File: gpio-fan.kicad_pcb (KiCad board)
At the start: 2 copper layers, 36 x 30.8 mm, 38 parts, among them J1 Conn_01x05, J10 Conn_01x04 DNS, J2 Conn_01x05 DNS, J3 Conn_01x02, J4 Conn_02x07_Odd_Even, J5 Conn_01x04 DNS, J6 Conn_01x02, J7 Conn_01x02 DNS, J8 Conn_01x02 DNS, J9 Conn_01x04 DNS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

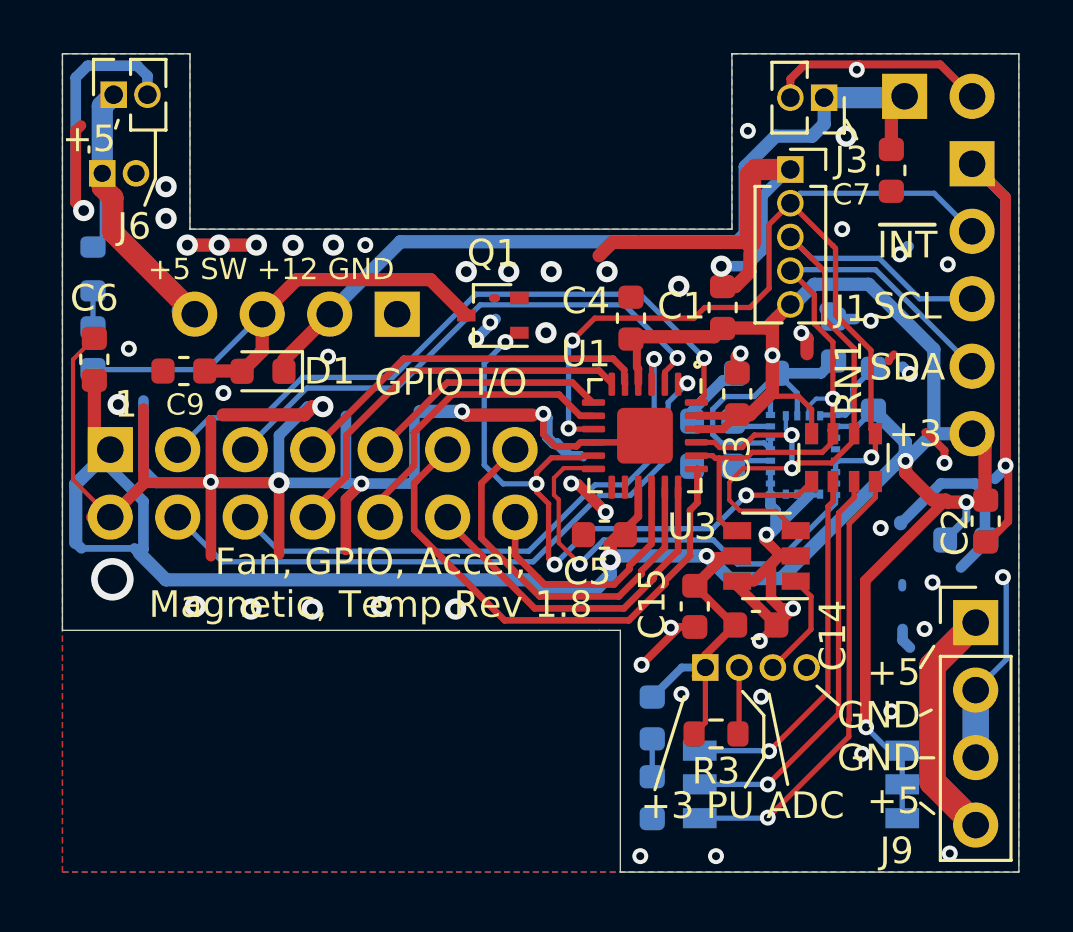
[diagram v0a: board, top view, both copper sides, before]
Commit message: V1.9, changed U2 to Bosch BMX180
Signed-off-by: Aaron Williams <aaron.w2@gmail.com>
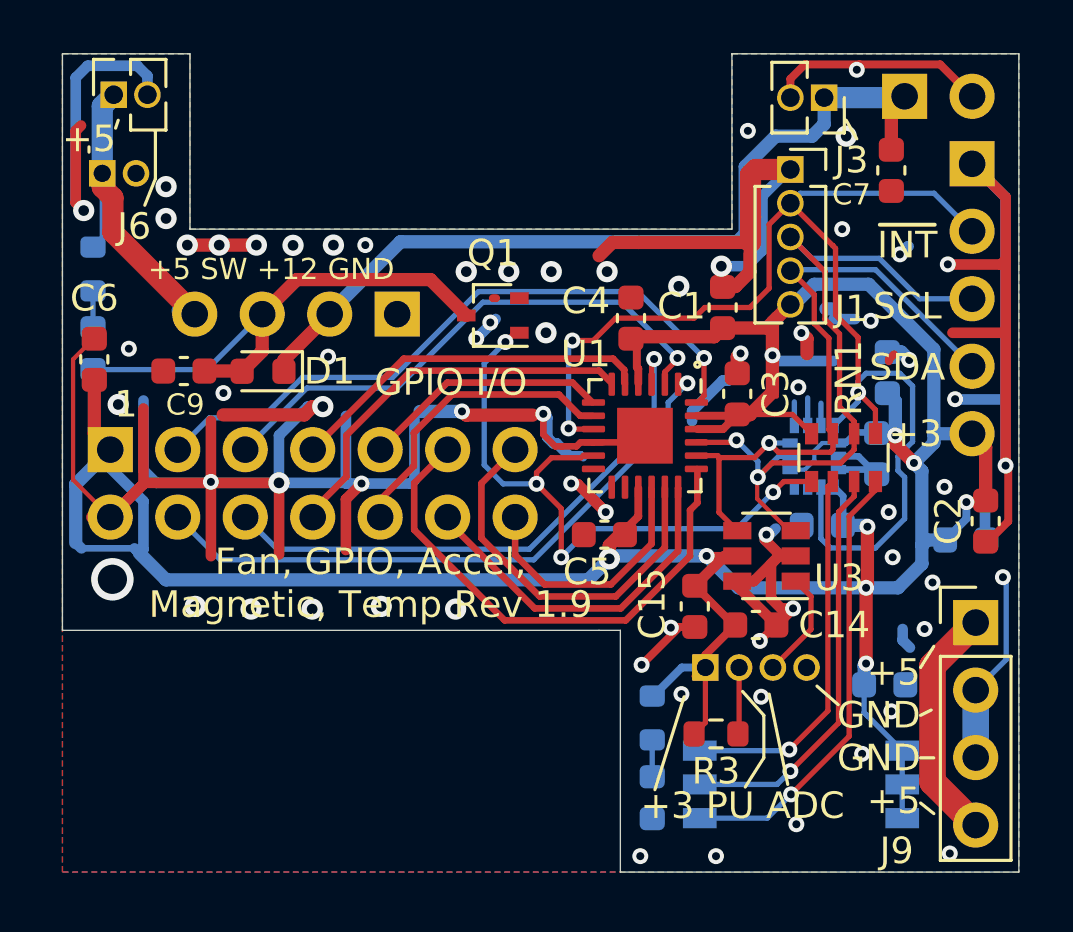
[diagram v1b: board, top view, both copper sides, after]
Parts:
- removed C16: 0.1uF, Capacitor_SMD:C_0603_1608Metric
- C10: value 0.01uF -> 0.1uF
- U2: value LSM9DS1 -> BMX160; footprint Package_LGA:LGA-24L_3x3.5mm_P0.43mm -> Aaron:PQFN50P250X300X100-14N
- moved C10 10.5 mm to (81.0, 65.8), turned to 0 degrees
- moved C11 6.24 mm to (78.6, 59.8)
- moved C8 2.43 mm to (80.7, 57.0), turned to 270 degrees
- moved C12 2.37 mm to (81.0, 54.0)
- moved U2 0.43 mm to (78.3, 57.1)
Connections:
- C10 pad 1: Net-(C10-Pad1) -> +3V3
- U2 pad 1: +3V3 -> GND
- U2 pad 10: /~INT -> (no net)
- U2 pad 11: /~INT -> (no net)
- U2 pad 12: /~INT -> +3V3
- U2 pad 13: Net-(U1-Pad12) -> /SCL
- U2 pad 14: GND -> /SDA
- U2 pad 2: /SCL -> GND
- U2 pad 3: +3V3 -> GND
- U2 pad 4: /SDA -> /~INT
- U2 pad 5: GND -> +3V3
- U2 pad 7: +3V3 -> GND
- U2 pad 9: Net-(U2-Pad9) -> /~INT
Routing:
- net Net-(U1-Pad12): track 16.9 -> 0.00 mm, vias 1 -> 0
- net /~INT: track 36.8 -> 49.1 mm
- net +3V3: track 135.4 -> 128.9 mm, vias 6 -> 9
- net GND: track 186.8 -> 182.3 mm, vias 64 -> 68
- net /SCL: track 31.3 -> 28.4 mm
- net Net-(C10-Pad1): track 1.49 -> 0.00 mm
- net Net-(C16-Pad1): track 1.48 -> 0.00 mm
- net /P0_1: track 24.2 -> 23.5 mm
- net /P0_3: track 22.0 -> 21.3 mm
- net /FAN_CTL: track 25.0 -> 24.4 mm
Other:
- board text added: "Fan, GPIO, Accel, Magnetic, Temp Rev 1.9"
- board text removed: "Fan, GPIO, Accel, Magnetic, Temp Rev 1.8"
